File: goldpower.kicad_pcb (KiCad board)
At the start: 2 copper layers, 30 parts, among them K1 CONN_3, P1 CONN_4, U1 LM317T, U2 LM337T

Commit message: First working version
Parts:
- removed C5, C6: 100n, C1-1
- added D7: LED, LED-3MM, F.Cu at (139.7, 51.8)
- added D8: LED, LED-3MM, F.Cu at (139.7, 74.2)
- added R5: R, R3, F.Cu at (137.2, 43.7)
- added R6: R, R3, F.Cu at (137.2, 81.8)
- added SYM: Symbol_OSHW-Logo_CopperTop_Negative_07Jul2012, Symbol_OSHW-Logo_CopperTop_Negative_07Jul2012, F.Cu at (60.5, 95.5)
- D1, D2, D3, D4: footprint D3 -> D4
- K1: footprint PINHEAD1-3 -> AKL073-3
- L1, L2: footprint CV3-30PF -> HFSRA_C
- P1: footprint PIN_ARRAY_4x1 -> AKL073-4
- U1, U2: footprint TO220 -> TO-220_Neutral123_Horizontal
- moved K1 38.9 mm to (140.2, 62.5), turned to 90 degrees
- moved R2 38.7 mm to (134.0, 81.9), turned to 270 degrees
- moved R1 38.7 mm to (134.0, 43.8), turned to 90 degrees
- moved C10 38.4 mm to (119.9, 68.1), turned to 90 degrees
- moved C1 33.0 mm to (72.4, 47.0)
- moved C3 33.0 mm to (105.4, 47.0)
- moved U2 31.2 mm to (127.0, 78.2), turned to 180 degrees
- moved U1 31.0 mm to (127.0, 47.8), turned to 0 degrees
- moved C7 23.5 mm to (134.0, 51.4)
- moved C8 22.2 mm to (134.0, 74.3), turned to 270 degrees
- moved C9 18.2 mm to (119.9, 57.9), turned to 90 degrees
- moved R3 17.1 mm to (127.0, 54.0), turned to 180 degrees
- moved R4 17.0 mm to (127.0, 71.6)
- moved D5 10.2 mm to (127.0, 57.1), turned to 180 degrees
- moved D6 10.2 mm to (127.0, 68.6)
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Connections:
- C10 pad 2: N-000002 (its old number) -> N-000001
- C9 pad 1: N-0000010 (its old number) -> N-000009
- D5 pad 2: N-0000010 (its old number) -> N-000009
- D6 pad 1: N-000002 (its old number) -> N-000001
- K1 pad 1: N-0000010 (its old number) -> N-000001
- K1 pad 3: N-000002 (its old number) -> N-000009
- P1 pad 2: GND -> (no net)
- P1 pad 3: GND -> (no net)
- R3 pad 2: N-0000010 (its old number) -> N-000009
- R4 pad 1: N-000002 (its old number) -> N-000001
- U1 pad 2: N-0000010 (its old number) -> N-000009
- U2 pad 3: N-000002 (its old number) -> N-000001
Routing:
- net N-0000013: track 0.00 -> 51.8 mm
- net N-0000014: track 0.00 -> 49.9 mm
- net N-000009: track 0.00 -> 44.9 mm
- net N-0000010: track 0.00 -> 42.6 mm
- net N-0000011: track 0.00 -> 42.1 mm
- net N-000001: track 0.00 -> 38.5 mm
- net N-000002: track 0.00 -> 31.0 mm
- net N-0000012: track 0.00 -> 30.5 mm
- net N-000008: track 0.00 -> 25.5 mm
- net N-000007: track 0.00 -> 18.0 mm
- net N-000005: track 0.00 -> 4.10 mm
- net N-000006: track 0.00 -> 3.59 mm
- added copper zone on F.Cu, net GND
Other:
- board outline added: 99.8 x 80 mm
- board text added: "+"
- board text added: "-"
- board text added: "Crazy Audio"
- board text added: "http://www.crazy-audio.com"

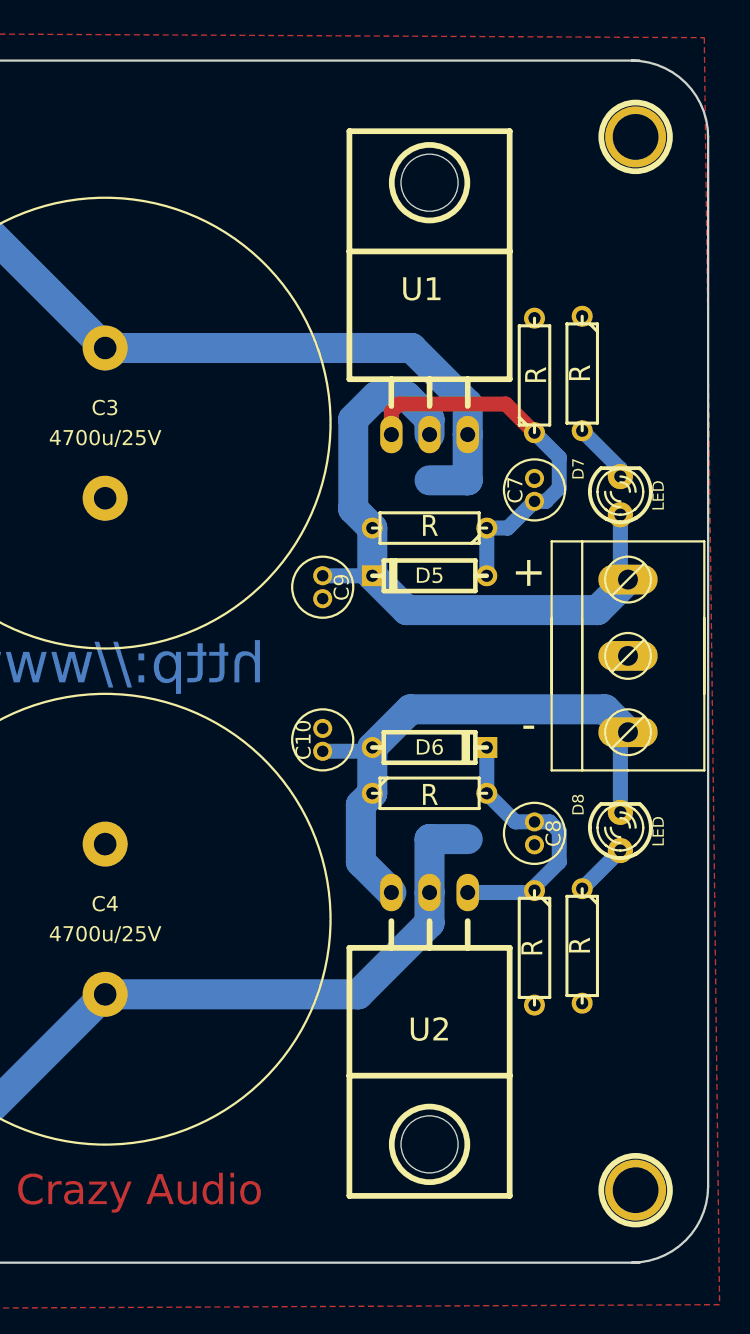
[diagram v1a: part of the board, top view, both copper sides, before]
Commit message: Slight changes, only 1 LED now
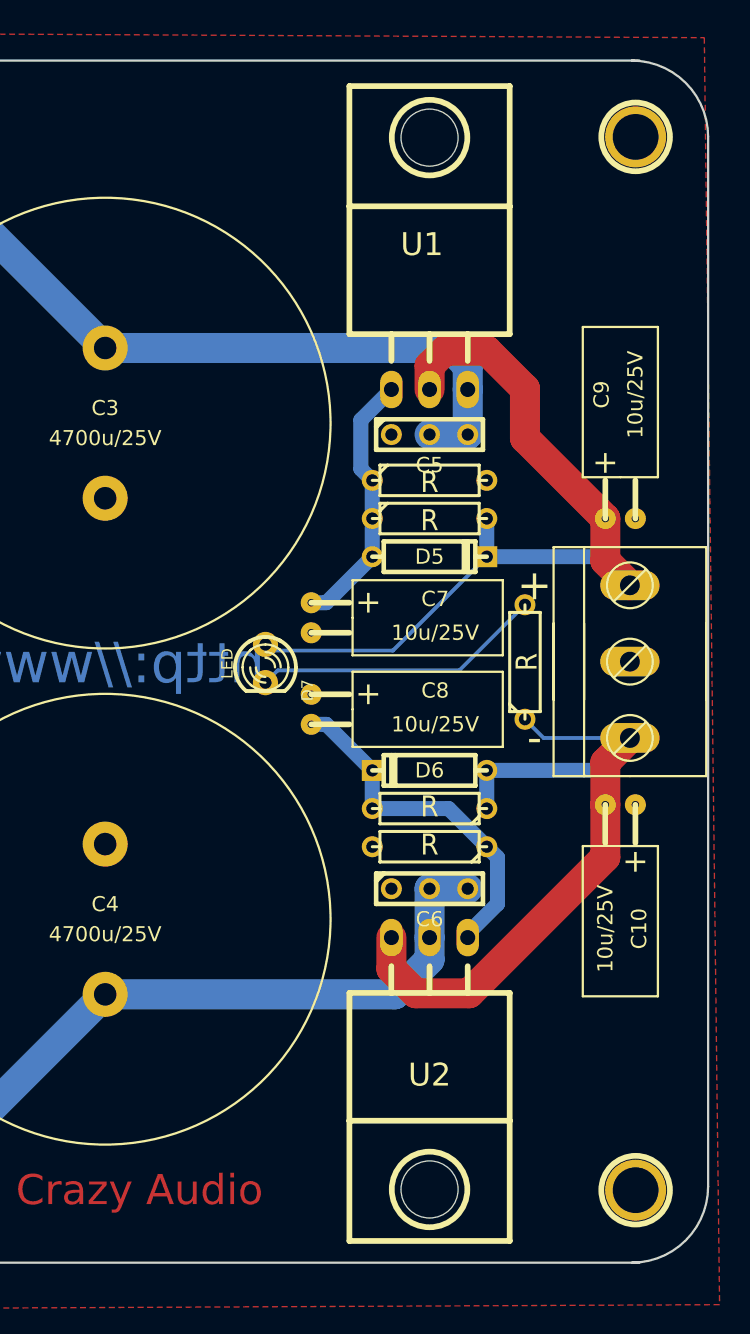
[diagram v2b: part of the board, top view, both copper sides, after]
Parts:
- removed D8: LED, LED-3MM
- removed R6: R, R3
- added C5: 100n, C1-1, F.Cu at (127.0, 47.8)
- added C6: 100n, C1-1, F.Cu at (127.0, 78.0)
- C10, C7, C8, C9: footprint CP_1.5_4 -> C2_D5x10
- moved D7 26.1 mm to (116.1, 63.0), turned to 270 degrees
- moved C9 20.3 mm to (139.7, 53.3), turned to 180 degrees
- moved C10 20.3 mm to (139.7, 72.4), turned to 0 degrees
- moved R5 19.6 mm to (133.3, 62.9), turned to 90 degrees
- moved C7 17.1 mm to (119.1, 59.9), turned to 90 degrees
- moved C8 17.0 mm to (119.1, 66.0), turned to 90 degrees
- moved R1 9.88 mm to (127.0, 50.8), turned to 0 degrees
- moved R2 9.70 mm to (127.0, 75.2), turned to 180 degrees
- moved U1 3.00 mm to (127.0, 44.8)
- moved U2 3.00 mm to (127.0, 81.2)
- moved D6 1.52 mm to (127.0, 70.1), turned to 180 degrees
- moved D5 1.27 mm to (127.0, 55.9), turned to 0 degrees
- moved R4 1.02 mm to (127.0, 72.6), turned to 180 degrees
- moved R3 0.63 mm to (127.0, 53.3), turned to 0 degrees
- moved K1 0.40 mm to (140.3, 62.9)
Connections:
- P1 pad 2: (no net) -> GND
- P1 pad 3: (no net) -> GND
- R5 pad 1: GND -> N-000001
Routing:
- net N-000004: track 4.10 -> 19.4 mm
- net N-000001: track 38.5 -> 49.8 mm
- net N-000005: track 44.9 -> 55.7 mm
- net N-000009: track 25.5 -> 17.6 mm
- net N-000003: track 18.0 -> 23.7 mm
- net N-000006 (its old number): track 3.59 -> 0.00 mm
- net N-0000011: track 49.9 -> 48.0 mm
- net N-0000010: track 51.8 -> 50.2 mm

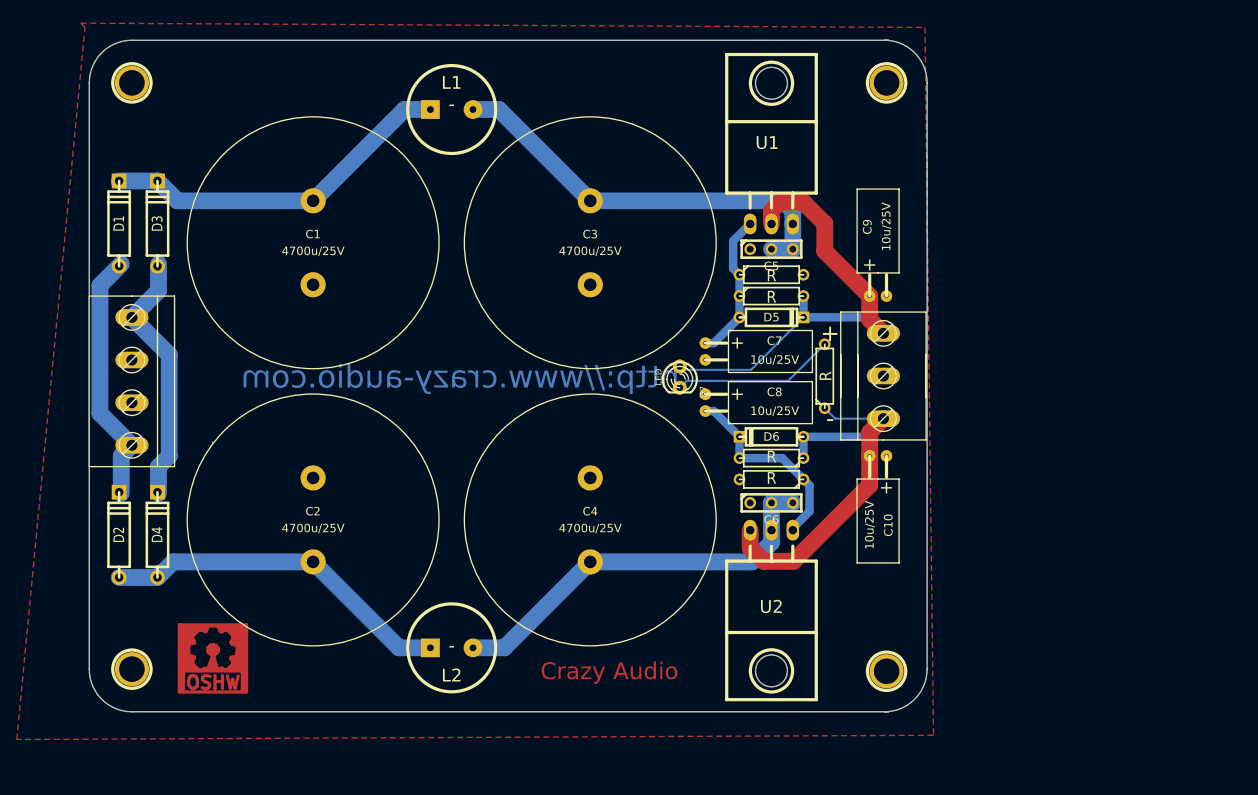
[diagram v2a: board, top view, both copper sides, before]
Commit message: two groundplanes now
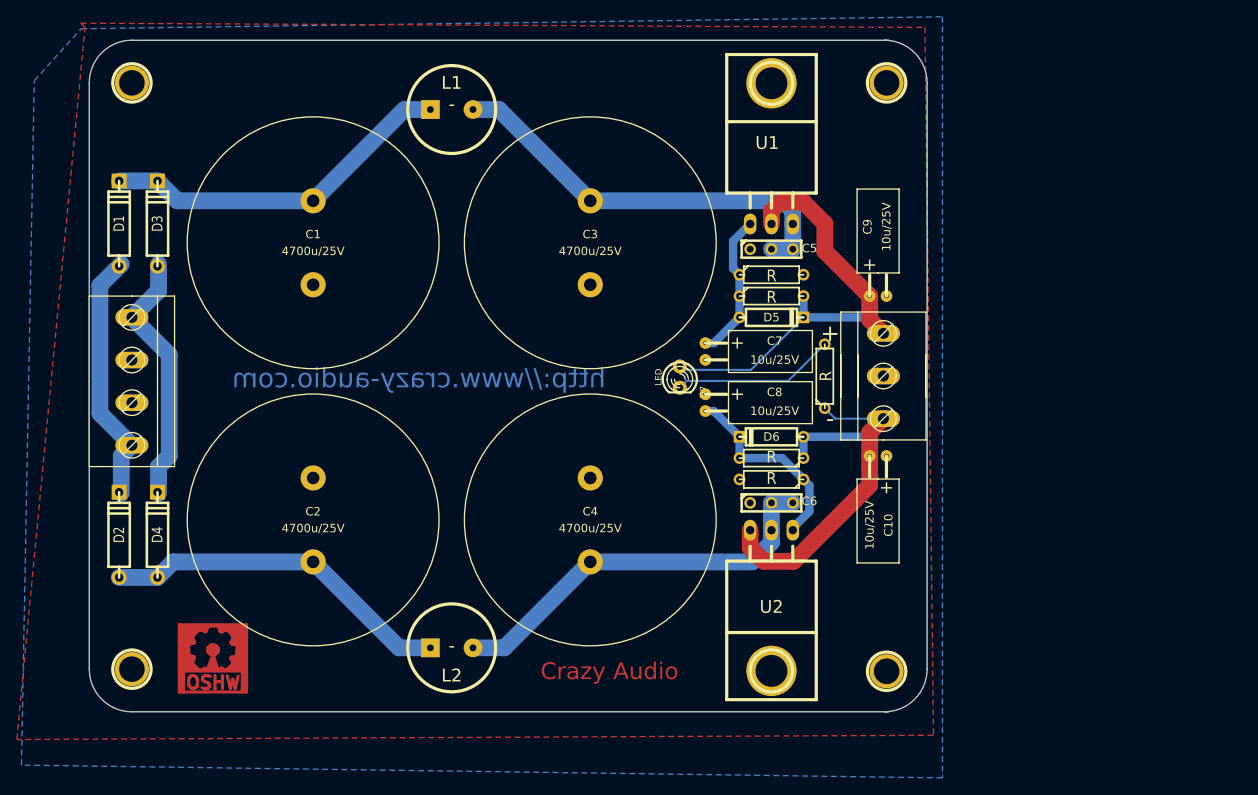
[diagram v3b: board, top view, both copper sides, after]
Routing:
- added copper zone on B.Cu, net GND
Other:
- outline, holes or cut-outs redrawn
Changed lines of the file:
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@@
     (links 51)
     (no_connects 0)
-    (area 22.25548 20.828 170.558333 111.22)
+    (area 22.25548 20.066 149.77745 110.744001)
     (thickness 1.6)
-    (drawings 15)
+    (drawings 12)
     (tracks 80)
     (zones 0)
@@
   (page A3)
   (layers
-    (15 F.Cu signal)
+    (15 F.Cu signal hide)
     (0 B.Cu signal)
     (16 B.Adhes user)
@@
     (visible_elements FFFFF7BF)
     (pcbplotparams
-      (layerselection 3178497)
+      (layerselection 284196865)
       (usegerberextensions true)
       (excludeedgelayer true)
@@
       (outputformat 1)
       (mirror false)
-      (drillshape 1)
+      (drillshape 0)
       (scaleselection 1)
       (outputdirectory ""))
@@
       (net 2 N-000001)
     )
-    (pad "" np_thru_hole circle (at 0 -16.764 270) (size 3.79984 3.79984) (drill 3.79984)
+    (pad "" thru_hole circle (at 0 -16.764 270) (size 6 6) (drill 3.79984)
       (layers *.Cu *.Mask F.SilkS)
     )
@@
       (net 3 N-0000010)
     )
-    (pad "" np_thru_hole circle (at 0 -16.764 90) (size 3.79984 3.79984) (drill 3.79984)
+    (pad "" thru_hole circle (at 0 -16.764 90) (size 6 6) (drill 3.79984)
       (layers *.Cu *.Mask F.SilkS)
     )
@@
     (descr "Condensateur e = 1 ou 2 pas")
     (tags C)
-    (fp_text reference C5 (at 0 2.032) (layer F.SilkS)
+    (fp_text reference C5 (at 4.5212 -0.1016) (layer F.SilkS)
       (effects (font (size 1.016 1.016) (thickness 0.2032)))
     )
@@
     (descr "Condensateur e = 1 ou 2 pas")
     (tags C)
-    (fp_text reference C6 (at 0 2.032) (layer F.SilkS)
+    (fp_text reference C6 (at 4.5212 -0.2032) (layer F.SilkS)
       (effects (font (size 1.016 1.016) (thickness 0.2032)))
     )
@@
     (effects (font (size 2 2) (thickness 0.3)) (justify mirror))
   )
-  (gr_text http://www.crazy-audio.com (at 89.916 62.992) (layer B.Cu)
-    (effects (font (size 2.7 2.7) (thickness 0.25)) (justify mirror))
+  (gr_text http://www.crazy-audio.com (at 84.9884 63.1444) (layer B.Cu)
+    (effects (font (size 2.3 2.3) (thickness 0.25)) (justify mirror))
   )
   (gr_line (start 145.542 97.79) (end 145.542 27.94) (angle 90) (layer Edge.Cuts) (width 0.15))
@@
   (gr_arc (start 50.8 97.79) (end 50.8 102.87) (angle 90) (layer Edge.Cuts) (width 0.15))
   (gr_arc (start 50.8 27.94) (end 45.72 27.94) (angle 90) (layer Edge.Cuts) (width 0.15))
-  (dimension 100.33 (width 0.25) (layer Eco2.User)
-    (gr_text "100.330 mm" (at 95.885 110.219999) (layer Eco2.User)
-      (effects (font (size 1 1) (thickness 0.25)))
-    )
-    (feature1 (pts (xy 45.72 102.87) (xy 45.72 111.219999)))
-    (feature2 (pts (xy 146.05 102.87) (xy 146.05 111.219999)))
-    (crossbar (pts (xy 146.05 109.219999) (xy 45.72 109.219999)))
-    (arrow1a (pts (xy 45.72 109.219999) (xy 46.846503 108.633579)))
-    (arrow1b (pts (xy 45.72 109.219999) (xy 46.846503 109.806419)))
-    (arrow2a (pts (xy 146.05 109.219999) (xy 144.923497 108.633579)))
-    (arrow2b (pts (xy 146.05 109.219999) (xy 144.923497 109.806419)))
-  )
-  (dimension 80.01 (width 0.25) (layer Eco2.User)
-    (gr_text "80.010 mm" (at 166.099999 62.865001 270) (layer Eco2.User)
-      (effects (font (size 1 1) (thickness 0.25)))
-    )
-    (feature1 (pts (xy 146.05 102.87) (xy 167.099999 102.870001)))
-    (feature2 (pts (xy 146.05 22.86) (xy 167.099999 22.860001)))
-    (crossbar (pts (xy 165.099999 22.860001) (xy 165.099999 102.870001)))
-    (arrow1a (pts (xy 165.099999 102.870001) (xy 164.513579 101.743498)))
-    (arrow1b (pts (xy 165.099999 102.870001) (xy 165.686419 101.743498)))
-    (arrow2a (pts (xy 165.099999 22.860001) (xy 164.513579 23.986504)))
-    (arrow2b (pts (xy 165.099999 22.860001) (xy 165.686419 23.986504)))
-  )
-  (gr_line (start 60.452 70.739) (end 60.452 70.866) (angle 90) (layer Edge.Cuts) (width 0.15))
-  (segment (start 133.35 66.7004) (end 134.5946 67.945) (width 0.254) (layer B.Cu) (net 2) (status 400000))
-  (segment (start 134.5946 67.945) (end 140.335 67.945) (width 0.254) (layer B.Cu) (net 2) (status 800000))
+  (segment (start 133.35 66.7004) (end 134.5946 67.945) (width 0.254) (layer B.Cu) (net 2))
+  (segment (start 134.5946 67.945) (end 140.335 67.945) (width 0.254) (layer B.Cu) (net 2))
   (segment (start 130.81 70.104) (end 130.81 72.644) (width 1) (layer B.Cu) (net 2))
   (segment (start 130.81 70.104) (end 138.176 70.104) (width 1) (layer B.Cu) (net 2))
@@
   (segment (start 131.5212 78.994) (end 131.5212 75.8952) (width 1) (layer B.Cu) (net 6))
   (segment (start 131.5212 75.8952) (end 130.81 75.184) (width 1) (layer B.Cu) (net 6))
-  (segment (start 133.35 59.0804) (end 128.9812 63.4492) (width 0.254) (layer B.Cu) (net 7) (status 400000))
-  (segment (start 116.8908 63.4492) (end 116.078 64.262) (width 0.254) (layer B.Cu) (net 7) (status 800000))
+  (segment (start 133.35 59.0804) (end 128.9812 63.4492) (width 0.254) (layer B.Cu) (net 7))
+  (segment (start 116.8908 63.4492) (end 116.078 64.262) (width 0.254) (layer B.Cu) (net 7))
   (segment (start 128.9812 63.4492) (end 116.8908 63.4492) (width 0.254) (layer B.Cu) (net 7))
   (segment (start 116.078 61.722) (end 116.4844 62.1284) (width 0.254) (layer B.Cu) (net 8))
@@
       )
     )
+  )
+  (zone (net 1) (net_name GND) (layer B.Cu) (hatch edge 0.508)
+    (connect_pads (clearance 0.254))
+    (min_thickness 0.254)
+    (fill (arc_segments 16) (thermal_gap 0.508) (thermal_bridge_width 0.508))
+    (polygon
+      (pts
+        (xy 147.3708 110.744) (xy 37.6428 109.22) (xy 39.1668 27.686) (xy 44.7548 21.4884) (xy 147.3708 20.066)
+        (xy 147.3708 110.744)
+      )
+    )
